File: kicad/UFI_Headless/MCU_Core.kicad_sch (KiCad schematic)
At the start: 61 parts, among them J4 SWD, J5 DBG_UART, J9 EXPANSION, SW1 RESET, SW2 BOOT, SW3 BTN_A, SW4 BTN_B, U11 APS6404L-3SQR-SN, U15 CSNP32GCR01-AOW, U5 STM32H723ZGT6, Y1 25MHz CL=12pF

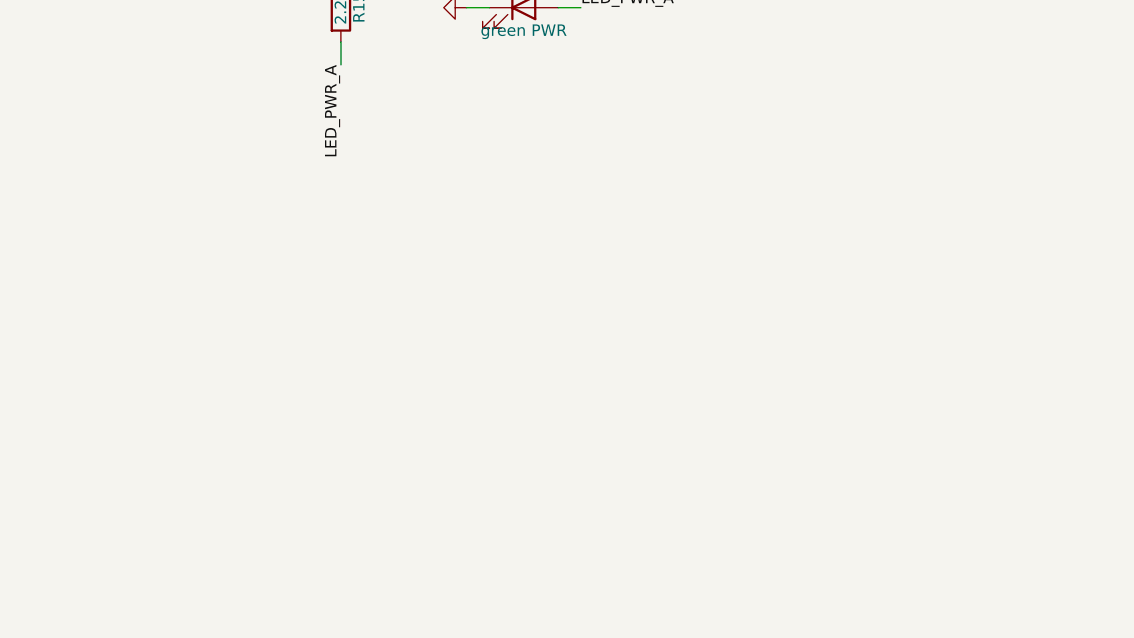
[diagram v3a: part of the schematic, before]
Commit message: v0.6: front panel LED header J12 (2x4, one row per LED) with 330R R34-R37
Enclosure LEDs: 1+/2- PWR (3V3), 3+/4- ACT, 5+/6- FDD, 7+/8- ERR, parallel to the
board LEDs (~4 mA each), no firmware change. Placed top left (22, 9), ECO re-route;
resistor references hidden (new eco/hide_ref.py), '12V DC' label re-placed.
DRC 0 incl. warnings, 0 unconnected, parity clean, no via-in-pad; fab outputs,
README, ordering guide (J12 hand-sourced) and bring-up step 4.6a updated.
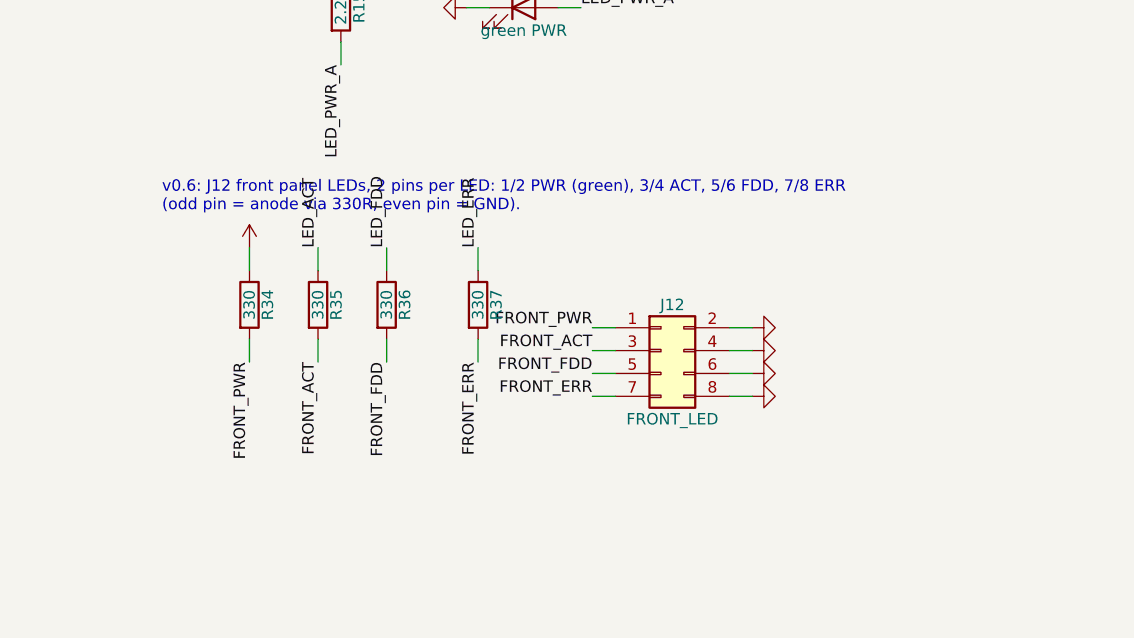
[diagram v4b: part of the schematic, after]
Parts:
- added J12: FRONT_LED, Connector_PinHeader_2.54mm:PinHeader_2x04_P2.54mm_Vertical, symbol Connector_Generic:Conn_02x04_Odd_Even
- added R34, R35, R36, R37: 330, Resistor_SMD:R_0603_1608Metric, symbol Device:R
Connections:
- net +3V3: now also R34.1
- net GND: now also J12.2 (Pin_2), J12.4 (Pin_4), J12.6 (Pin_6), J12.8 (Pin_8)
- net LED_ACT: now also R35.1
- net LED_ERR: now also R37.1
- net LED_FDD: now also R36.1
- new net FRONT_ACT: J12.3 (Pin_3), R35.2
- new net FRONT_ERR: J12.7 (Pin_7), R37.2
- new net FRONT_FDD: J12.5 (Pin_5), R36.2
- new net FRONT_PWR: J12.1 (Pin_1), R34.2
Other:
- note added: "v0.6: J12 front panel LEDs, 2 pins per LED: 1/2 PWR (green), 3/4 ACT, 5/6 FDD, 7/8 ERR (odd pin = anode via 330R, even pin = GND)."

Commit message: v0.6: mode switch header J13; firmware 1.5: Shugart bus DS0-DS3 (4 drives), UFI.CFG
Board: J13 1x3 (pin order = ON-OFF-ON toggle switch: 1 floppy, 2 common 3V3, 3 SD),
parallel to J9 pins 5/6, placed top left (21, 21), ECO re-route, 'MODE 1=FLOP 3=SD'
label; DRC 0 incl. warnings, 0 unconnected, parity clean, no via-in-pad.

Firmware 1.5:
- Shugart bus drive types DS0-DS3 (6-9): select on pins 10/12/14/6 (pin 6 = DRATE line
  through JP1), shared MOTOR ON pin 16; existing type numbers unchanged
- UFI.CFG on the SD NAND (created with defaults): stand-alone drive for dump and USB
  floppy (a/b/amiga/ds0-ds3) and dump tracks/sides/revs; parser tested on the host
- host: drive names ds0-ds3
- docs: J6 Shugart bus (corrects the old 'firmware picks the bus type' claim), J13,
  UFI.CFG, bring-up steps 7.2a/7.2b
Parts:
- added J13: MODE_SW, Connector_PinHeader_2.54mm:PinHeader_1x03_P2.54mm_Vertical, symbol Connector_Generic:Conn_01x03
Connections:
- net +3V3: now also J13.2 (Pin_2)
- net EXP_IO1: now also J13.1 (Pin_1)
- net EXP_IO2: now also J13.3 (Pin_3)
